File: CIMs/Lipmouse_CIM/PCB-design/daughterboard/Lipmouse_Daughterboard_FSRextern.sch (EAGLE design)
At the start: 9 parts

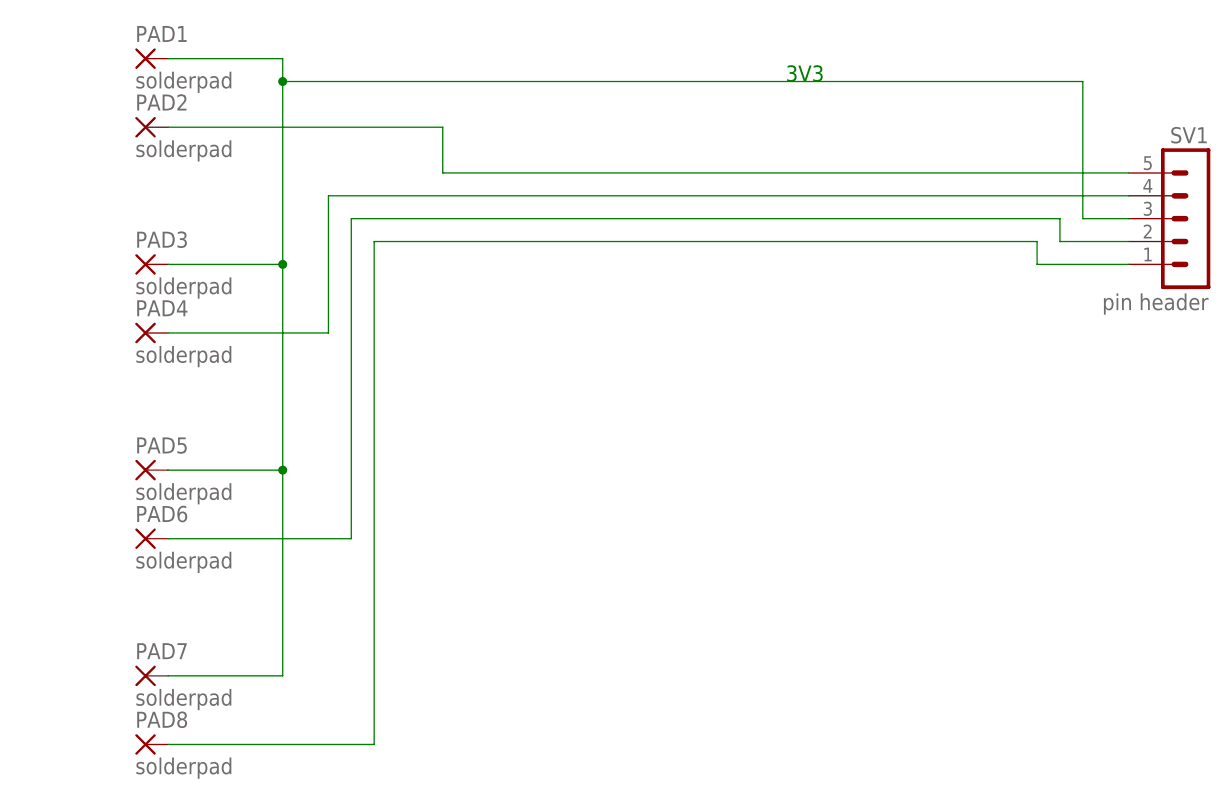
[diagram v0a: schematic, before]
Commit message: Update Lipsy (Lipmouse) PCB and case designs
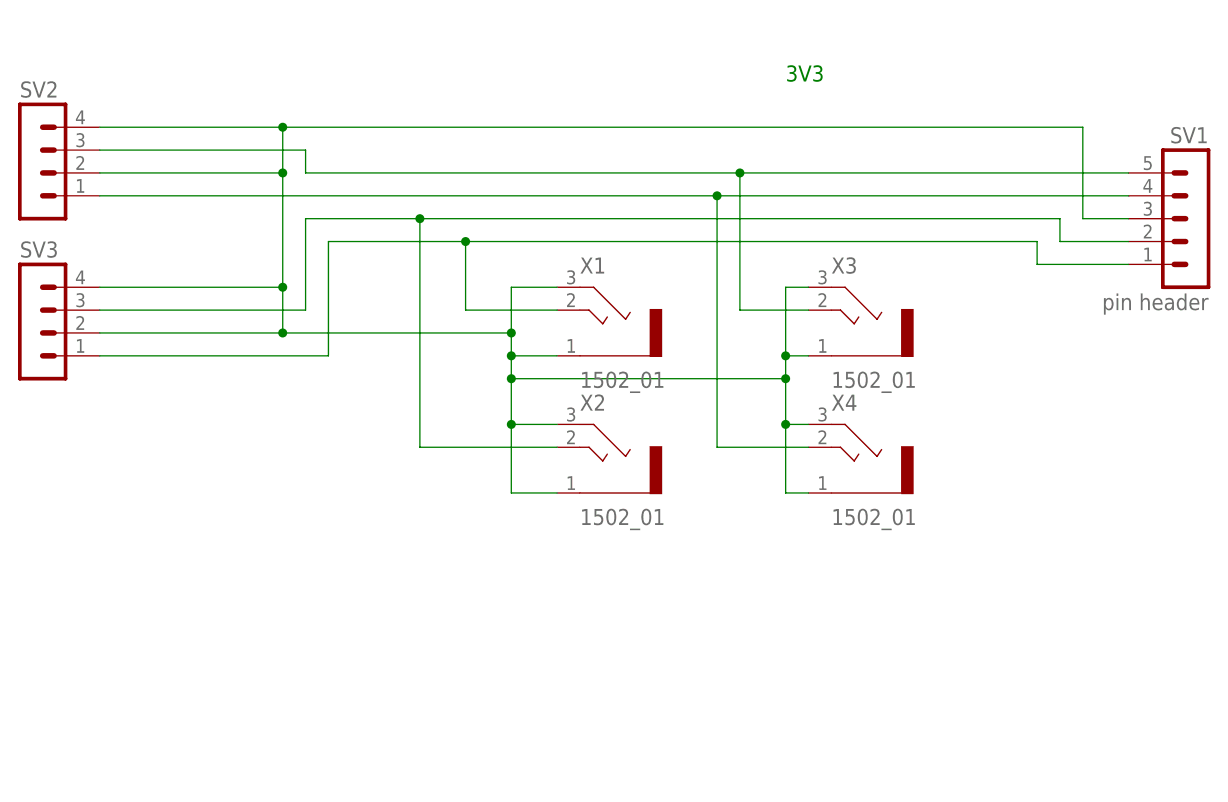
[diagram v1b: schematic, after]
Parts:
- removed PAD1, PAD2, PAD3, PAD4, PAD5, PAD6, PAD7, PAD8: solderpad, wirepad:SMD5
- added SV2, SV3: (no value), con-lstb:MA04-1
- added X1, X2, X3, X4: 1502_01, con-lumberg:1502_01
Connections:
- removed net N$20: PAD2.P, SV1.5
- removed net N$21: PAD4.P, SV1.4
- new net N$1: SV1.4, SV2.1, X4.3
- new net N$2: SV1.5, SV2.3, X3.3
- net 3V3: now also SV2.2, SV2.4, SV3.2, SV3.4, X1.1, X1.2, X2.1, X2.2, X3.1, X3.2, X4.1, X4.2; no longer PAD1.P, PAD3.P, PAD5.P, PAD7.P
- net N$22: now also SV3.3, X2.3; no longer PAD6.P
- net N$23: now also SV3.1, X1.3; no longer PAD8.P
